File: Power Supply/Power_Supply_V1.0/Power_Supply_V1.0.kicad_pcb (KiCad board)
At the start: 2 copper layers, 158.8 x 72.4 mm, 40 parts

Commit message: Updated Gerber
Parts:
- moved TP2 3.87 mm to (144.2, 123.5)
- moved R3 3.86 mm to (152.3, 123.5)
- moved R4 3.86 mm to (180.2, 123.5)
- moved REF** 1.33 mm to (65.7, 132.5)
- moved REF** 1.31 mm to (215.8, 132.5)
- moved TP6 1.18 mm to (79.1, 132.6)
- moved TP9 1.18 mm to (72.8, 132.6)
- moved TP4 1.00 mm to (176.4, 132.7)
- moved TP3 1.00 mm to (148.6, 132.7)
- moved TP5 1.00 mm to (204.2, 132.7)
- moved TP7 1.00 mm to (122.2, 132.7)
- moved TP8 1.00 mm to (115.7, 132.7)
- moved C8 0.74 mm to (131.9, 126.2)
- moved REF** 0.17 mm to (215.8, 70.0)
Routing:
- net C: track 27.7 -> 20.7 mm
- net B: track 27.9 -> 21.4 mm
- net D: track 20.0 -> 16.1 mm
- net Net-(D2-K): track 49.6 -> 47.4 mm
- net Net-(C8-Pad2): track 24.2 -> 22.2 mm
- net F: track 31.5 -> 29.7 mm
- net G: track 28.8 -> 27.2 mm
- net GND: track 239.3 -> 240.8 mm
- net 60VAC: track 13.0 -> 11.7 mm
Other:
- board size 158.8 x 72.4 mm -> 158.8 x 71.1 mm

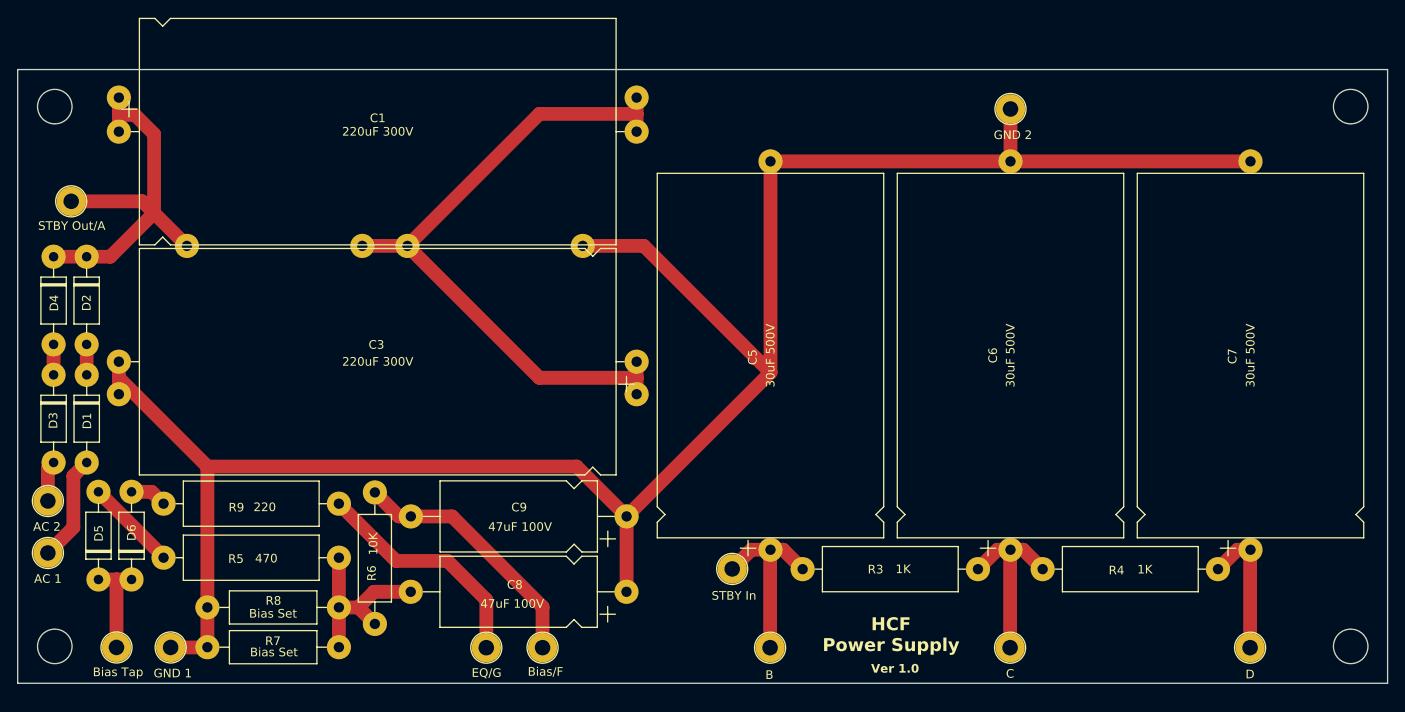
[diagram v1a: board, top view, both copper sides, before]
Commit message: Condensed Reservoir Caps
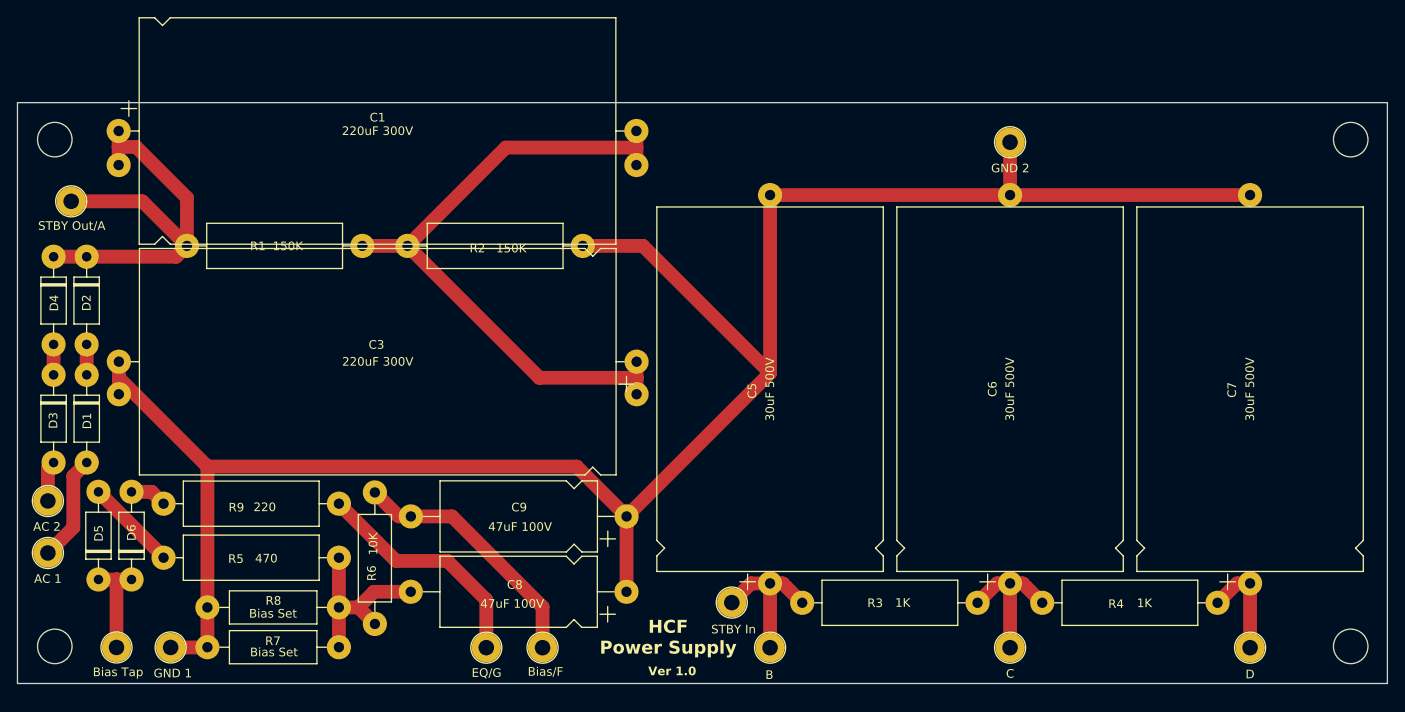
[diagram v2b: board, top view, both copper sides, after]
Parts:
- R1, R2: moved to F.Cu
- moved C2 7.82 mm to (73.1, 76.7)
- moved C5 3.90 mm to (148.6, 125.2)
- moved C6 3.90 mm to (176.4, 125.2)
- moved C7 3.90 mm to (204.2, 125.2)
- moved R3 3.90 mm to (152.3, 127.5)
- moved R4 3.90 mm to (180.1, 127.5)
- moved TP2 3.90 mm to (144.1, 127.4)
- moved TP12 3.85 mm to (176.4, 74.1)
- moved REF** 3.83 mm to (215.8, 73.8)
- moved REF** 3.83 mm to (65.7, 73.8)
- moved C1 0.08 mm to (73.1, 72.8)
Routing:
- net Net-(D2-K): track 47.4 -> 51.4 mm
- net C: track 20.7 -> 16.8 mm
- net B: track 21.4 -> 17.5 mm
- net D: track 16.1 -> 12.2 mm
- net GND: track 240.8 -> 236.9 mm
- net Net-(C1-Pad2): track 78.7 -> 77.1 mm
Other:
- board size 158.8 x 71.1 mm -> 158.8 x 67.3 mm

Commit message: increased ground trace in PSV1.0
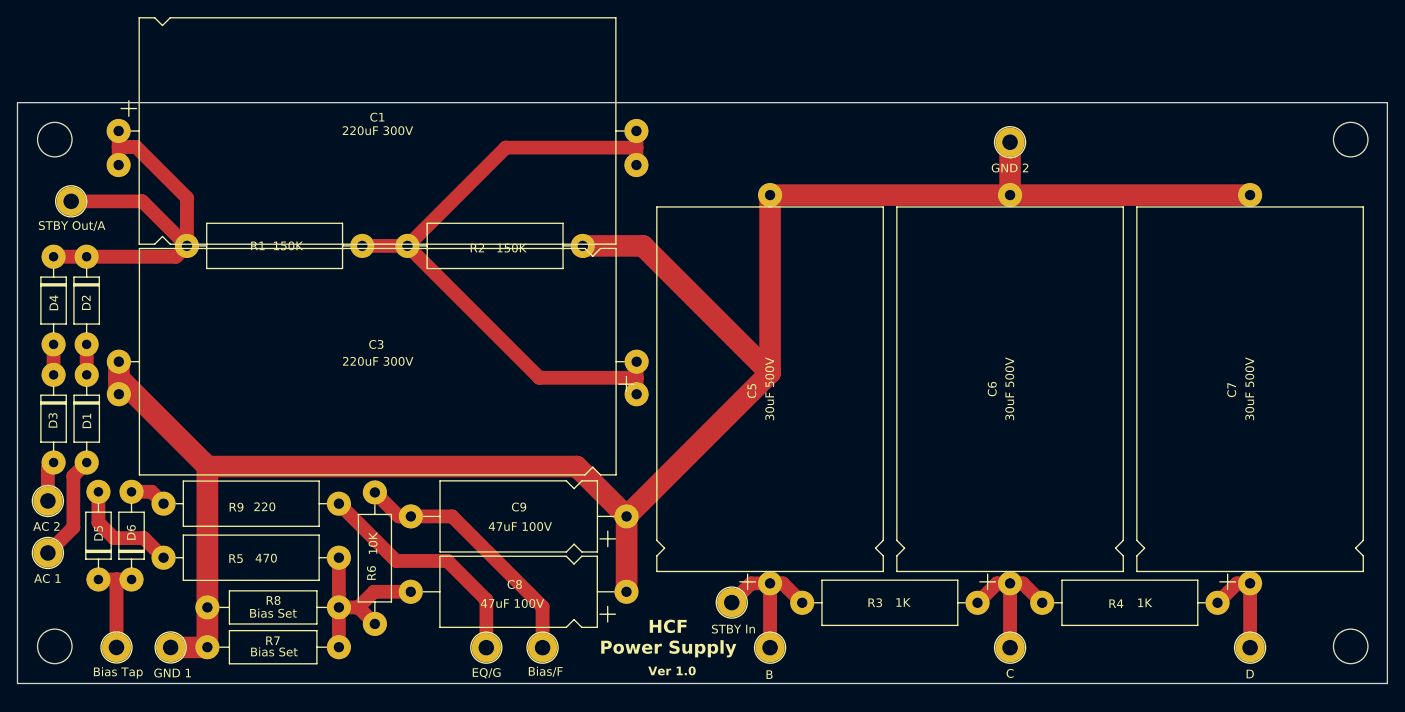
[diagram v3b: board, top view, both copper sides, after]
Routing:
- net Net-(D5-A): track 10.8 -> 12.8 mm
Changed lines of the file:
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@@
 		(start 126.86 86.0925)
 		(end 133.8395 86.0925)
-		(width 1.6)
+		(width 2.5)
 		(layer "F.Cu")
 		(net 3)
@@
 		(start 133.8395 86.0925)
 		(end 148.562 100.815)
-		(width 1.6)
+		(width 2.5)
 		(layer "F.Cu")
 		(net 3)
@@
 		(start 73.1 101.4)
 		(end 73.1 103.28)
-		(width 1.6)
+		(width 2.5)
 		(layer "F.Cu")
 		(net 3)
@@
 		(start 148.562 80.2)
 		(end 176.375 80.2)
-		(width 1.6)
+		(width 2.5)
 		(layer "F.Cu")
 		(net 3)
@@
 		(start 176.375 80.2)
 		(end 176.375 74.075)
-		(width 1.6)
+		(width 2.5)
 		(layer "F.Cu")
 		(net 3)
@@
 		(start 83.3595 111.6595)
 		(end 83.3595 127.985)
-		(width 1.6)
+		(width 2.5)
 		(layer "F.Cu")
 		(net 3)
@@
 		(start 83.3595 127.985)
 		(end 83.3595 132.595)
-		(width 1.6)
+		(width 2.5)
 		(layer "F.Cu")
 		(net 3)
@@
 		(start 176.375 80.2)
 		(end 204.188 80.2)
-		(width 1.6)
+		(width 2.5)
 		(layer "F.Cu")
 		(net 3)
@@
 		(start 73.1 99.51)
 		(end 73.1 101.4)
-		(width 1.6)
+		(width 2.5)
 		(layer "F.Cu")
 		(net 3)
@@
 		(start 79.1 132.625)
 		(end 83.3295 132.625)
-		(width 1.6)
+		(width 2.5)
 		(layer "F.Cu")
 		(net 3)
@@
 		(start 148.562 80.2)
 		(end 148.562 100.815)
-		(width 1.6)
+		(width 2.5)
 		(layer "F.Cu")
 		(net 3)
@@
 		(start 148.562 100.815)
 		(end 131.937 117.44)
-		(width 1.6)
+		(width 2.5)
 		(layer "F.Cu")
 		(net 3)
@@
 		(start 131.937 126.163)
 		(end 131.925 126.175)
-		(width 1.6)
+		(width 2.5)
 		(layer "F.Cu")
 		(net 3)
@@
 		(start 73.1 101.4)
 		(end 83.3595 111.6595)
-		(width 1.6)
+		(width 2.5)
 		(layer "F.Cu")
 		(net 3)
@@
 		(start 131.937 117.44)
 		(end 131.937 126.163)
-		(width 1.6)
+		(width 2.5)
 		(layer "F.Cu")
 		(net 3)
@@
 		(start 83.3295 132.625)
 		(end 83.3595 132.595)
-		(width 1.6)
+		(width 2.5)
 		(layer "F.Cu")
 		(net 3)
@@
 		(start 126.1565 111.6595)
 		(end 131.937 117.44)
-		(width 1.6)
+		(width 2.5)
 		(layer "F.Cu")
 		(net 3)
@@
 		(start 83.3595 111.6595)
 		(end 126.1565 111.6595)
-		(width 1.6)
+		(width 2.5)
 		(layer "F.Cu")
 		(net 3)
@@
 	)
 	(segment
-		(start 78.2795 122.13375)
+		(start 70.73575 118.16075)
+		(end 72.525 119.95)
+		(width 1.6)
+		(layer "F.Cu")
+		(net 13)
+	)
+	(segment
+		(start 72.525 119.95)
+		(end 76.0045 119.95)
+		(width 1.6)
+		(layer "F.Cu")
+		(net 13)
+	)
+	(segment
+		(start 76.0045 119.95)
 		(end 78.2795 122.225)
 		(width 1.6)
@@
 	(segment
 		(start 70.73575 114.59)
-		(end 78.2795 122.13375)
-		(width 1.6)
-		(layer "F.Cu")
+		(end 70.73575 118.16075)
+		(width 1.6)
+		(layer "F.Cu")

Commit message: Added Solder Pads, Updated Power Supply Board
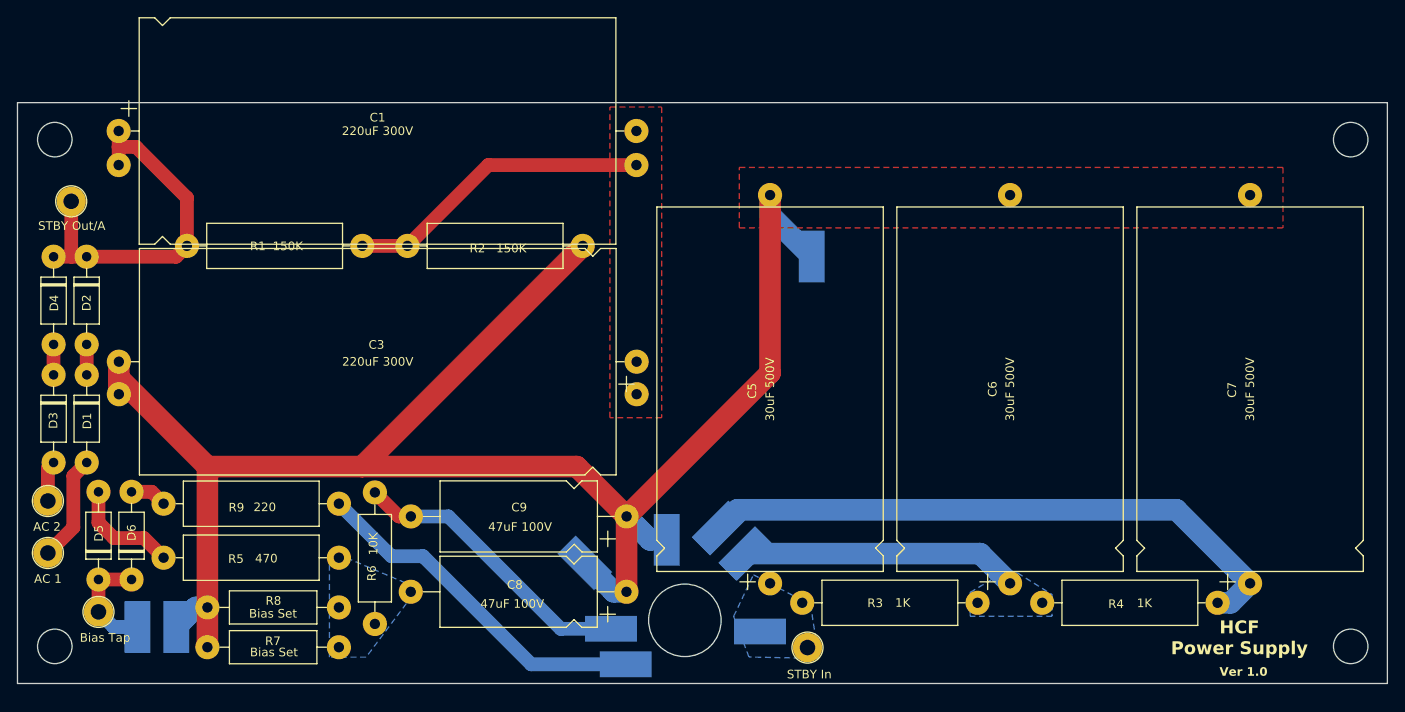
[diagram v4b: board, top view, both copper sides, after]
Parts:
- added REF**: MountingHole_8.4mm_M8, MountingHole:MountingHole_8.4mm_M8, F.Cu at (138.7, 129.5)
- added TP13: GND 3, HiroFootprints:WirePad, B.Cu at (127.3, 123.0)
- added TP14: GND 4, HiroFootprints:WirePad, B.Cu at (153.4, 87.6)
- added TP15: Bias Tap Out, HiroFootprints:WirePad, B.Cu at (75.2, 130.5)
- TP12, TP3, TP4, TP5, TP6, TP7, TP8: footprint HiroFootprints:Out_Hole_3.4_1.8 -> HiroFootprints:WirePad; moved to B.Cu
- moved TP5 63.2 mm to (142.5, 119.0), turned to 135 degrees
- moved TP12 60.7 mm to (136.6, 119.9)
- moved TP4 32.6 mm to (145.6, 121.9), turned to 135 degrees
- moved TP8 16.0 mm to (131.6, 134.6), turned to 90 degrees
- moved TP2 10.2 mm to (152.9, 132.6)
- moved TP7 8.47 mm to (130.4, 130.5), turned to -90 degrees
- moved TP9 4.62 mm to (70.7, 128.5)
- moved TP6 2.22 mm to (79.8, 130.5), turned to 180 degrees
- moved TP3 2.09 mm to (147.6, 130.8), turned to -90 degrees
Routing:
- net D: track 12.2 -> 70.6 mm
- net Net-(C1-Pad2): track 77.1 -> 35.6 mm
- net GND: track 236.9 -> 204.9 mm
- net Net-(C8-Pad2): track 22.2 -> 0.00 mm
- net B: track 17.5 -> 0.00 mm
- net C: track 16.8 -> 32.1 mm
- net G: track 27.2 -> 40.9 mm
- net Net-(D2-K): track 51.4 -> 42.3 mm
- net F: track 29.7 -> 33.9 mm
- net 60VAC: track 11.7 -> 12.8 mm
- added copper zone on B.Cu, net B
- added copper zone on B.Cu, net C
- added copper zone on F.Cu, net GND
- added copper zone on F.Cu, net Net-(C1-Pad2)
- added copper zone on B.Cu, net Net-(C8-Pad2)
